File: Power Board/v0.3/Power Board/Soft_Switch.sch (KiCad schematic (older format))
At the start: 13 parts

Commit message: power board v0.3 - Raspberry Pi side only
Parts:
- removed C?: 100nF, symbol Device:C
- removed C?: 10µF, symbol Device:C
- removed C?: 1µF, symbol Device:C
- removed D?: DIODE, symbol pspice:DIODE
- removed Q? (x2): IRF7319PbF, symbol Power_Board:IRF7319PbF
- removed R? (x2): 100K, symbol Device:R
- removed R?: 330K, symbol Device:R
- removed R?: 10K, symbol Device:R
- removed R?: 1K, symbol Device:R
- removed SW?: SW_Push, symbol Switch:SW_Push
- added C10: 10µF, Capacitor_SMD:C_1210_3225Metric, symbol Device:C
- added C8: 1µF, Capacitor_SMD:C_0805_2012Metric, symbol Device:C
- added C9: 100nF, Capacitor_SMD:C_0603_1608Metric, symbol Device:C
- added D2: BAT54C, Package_TO_SOT_SMD:SOT-23, symbol Diode:BAT54C
- added D3: LED, green, LED_SMD:LED_0603_1608Metric, symbol Device:LED
- added D4: LED, red, LED_SMD:LED_0603_1608Metric, symbol Device:LED
- added L1: 300R, Inductor_SMD:L_0603_1608Metric, symbol Device:L_Core_Ferrite_Small
- added Q1: SI5504BDC, symbol Power_Board:SI5504BDC
- added Q2: DMG2305UX-7, Package_TO_SOT_SMD:SOT-23, symbol Power_Board:DMG2305UX-7
- added R10, R8: 100K, Resistor_SMD:R_0603_1608Metric, symbol Device:R
- added R11, R13: 680, Resistor_SMD:R_0603_1608Metric, symbol Device:R
- added R12, R9: 330K, Resistor_SMD:R_0603_1608Metric, symbol Device:R
- added R7: 10K, Resistor_SMD:R_0603_1608Metric, symbol Device:R
- F1: renamed from F?; footprint (none) -> Package_TO_SOT_SMD:SOT-23
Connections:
- net labels added: Power_Button, Power_Ctl_GPIO, Power_Sense_GPIO
- net labels removed: Power_GPIO
- wire segments 37 -> 53
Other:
- note added: "Drive high to keep power on."
- note added: "Low when button pressed."
- note removed: "Input w/ pull-up to read button state.\nOutput LOW to power off.\n \n"
- moved on the sheet: F1

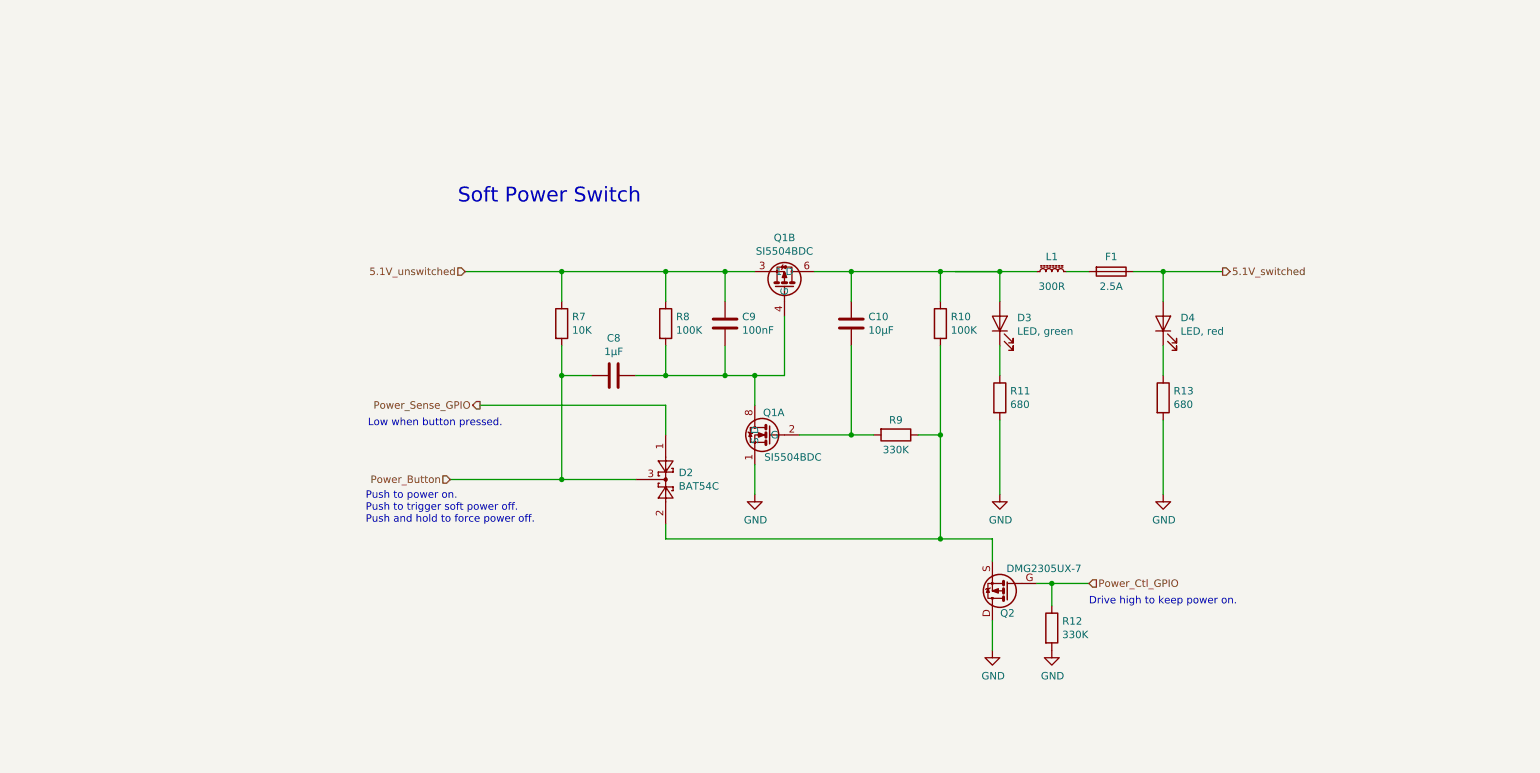
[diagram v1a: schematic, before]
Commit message: Revised soft power switch.  Now switches power to 5V regulator.
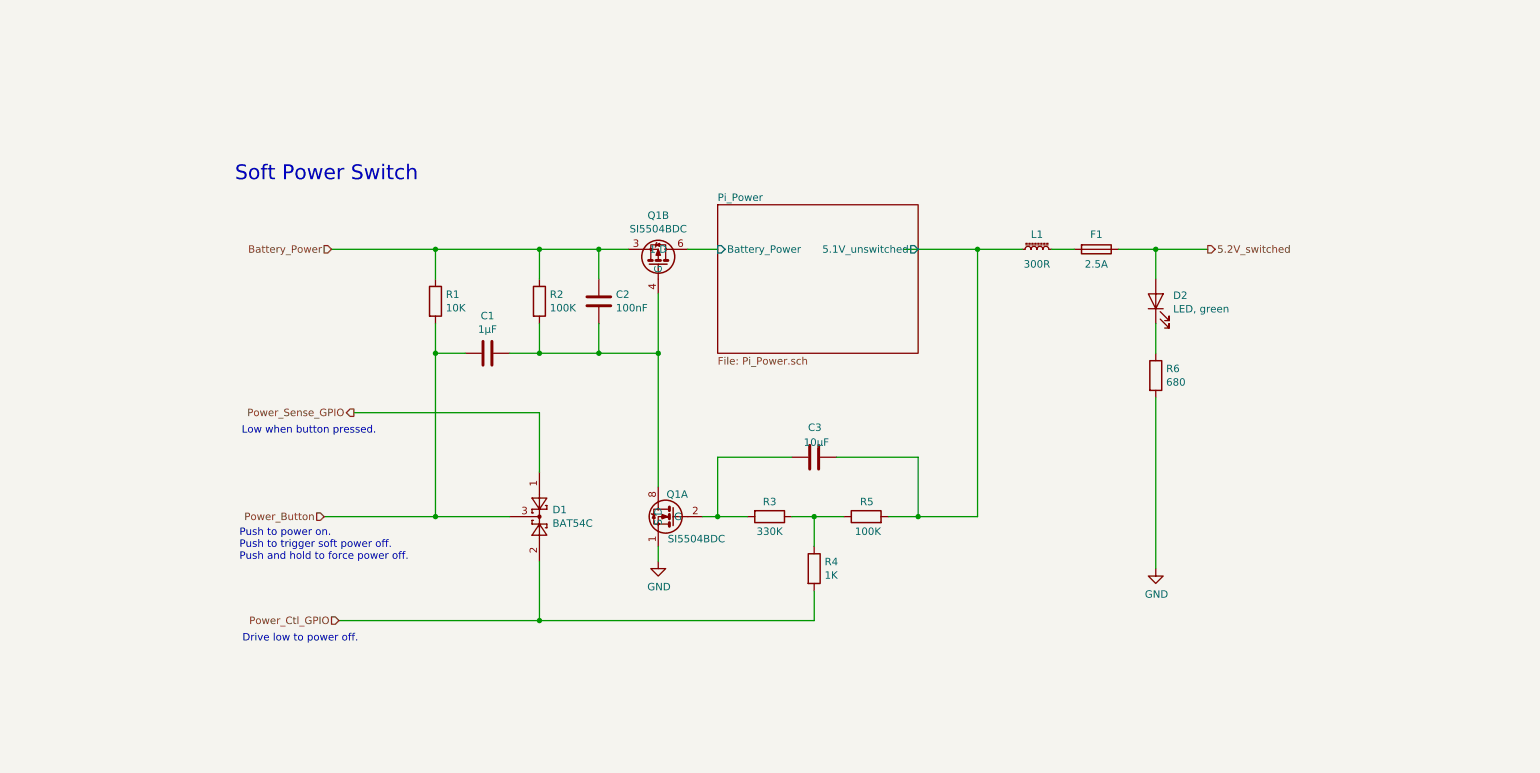
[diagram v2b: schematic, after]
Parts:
- removed D4: LED, red, LED_SMD:LED_0603_1608Metric, symbol Device:LED
- removed Q2: DMG2305UX-7, Package_TO_SOT_SMD:SOT-23, symbol Power_Board:DMG2305UX-7
- removed R12: 330K, Resistor_SMD:R_0603_1608Metric, symbol Device:R
- removed R13: 680, Resistor_SMD:R_0603_1608Metric, symbol Device:R
- added R4: 1K, Resistor_SMD:R_0603_1608Metric, symbol Device:R
- R3: renamed from R9; Part No. RX0603JR-07330K -> RC0603JR-07330K
- renumbered C8 to C1, C9 to C2, C10 to C3, D2 to D1, D3 to D2, R7 to R1, R8 to R2, R10 to R5, R11 to R6
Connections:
- net Power_Ctl_GPIO: now also D1.2, R4.2
- net at Q1.2 (G), R3.2: now also C3.1; no longer C3.2
- net 5.1V_switched renamed 5.2V_switched
- net 5.2V_switched: now also D2.2 (A)
- net 5.1V_unswitched renamed Battery_Power
- new net: C3.2, L1.1, R5.2
- new net: R3.1, R4.1, R5.1
- new net Pi_Power/Battery_Power: Q1.5 (D), Q1.6 (D)
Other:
- note added: "Drive low to power off."
- note removed: "Drive high to keep power on."
- moved on the sheet: C1, C2, C3, D1, D2, F1, L1, Q1A, Q1B, R1, R2, R3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

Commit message: Merge Pi_Power schematic into Soft_Switch.
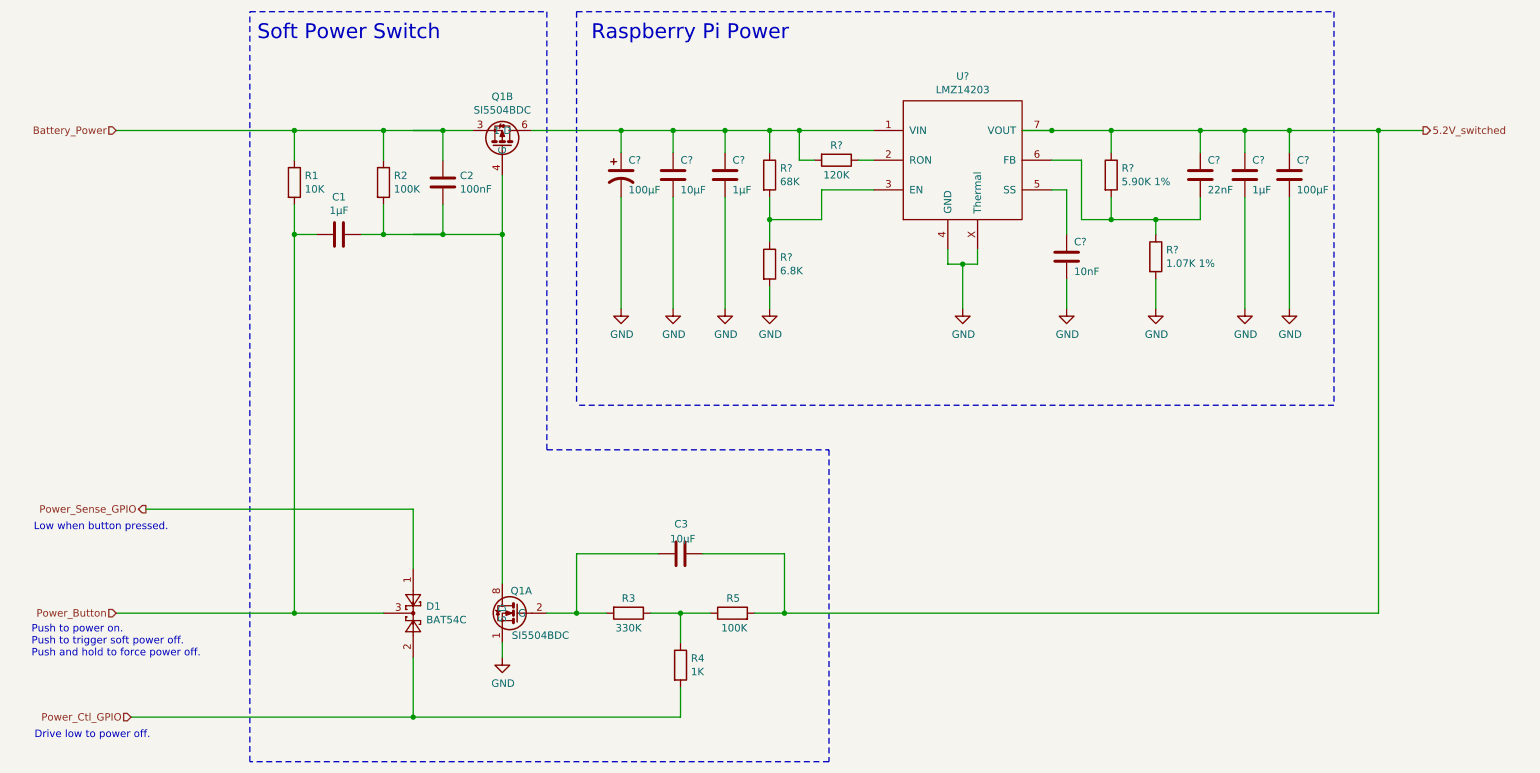
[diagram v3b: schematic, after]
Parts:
- removed D2: LED, green, LED_SMD:LED_0603_1608Metric, symbol Device:LED
- removed F1: 2.5A, Package_TO_SOT_SMD:SOT-23, symbol Device:Fuse
- removed L1: 300R, Inductor_SMD:L_0603_1608Metric, symbol Device:L_Core_Ferrite_Small
- removed R6: 680, Resistor_SMD:R_0603_1608Metric, symbol Device:R
- added C?: 10µF, Capacitor_SMD:C_1210_3225Metric, symbol Device:C
- added C? (x2): 1µF, Capacitor_SMD:C_0805_2012Metric, symbol Device:C
- added C?: 10nF, Capacitor_SMD:C_0603_1608Metric, symbol Device:C
- added C?: 22nF, Capacitor_SMD:C_0603_1608Metric, symbol Device:C
- added C?: 100µF, Capacitor_SMD:C_1210_3225Metric, symbol Device:C
- added C?: 100µF, symbol Device:CP1
- added R?: 1.07K 1%, Resistor_SMD:R_0603_1608Metric, symbol Device:R
- added R?: 5.90K 1%, Resistor_SMD:R_0603_1608Metric, symbol Device:R
- added R?: 6.8K, Resistor_SMD:R_0603_1608Metric, symbol Device:R
- added R?: 120K, Resistor_SMD:R_0603_1608Metric, symbol Device:R
- added R?: 68K, Resistor_SMD:R_0603_1608Metric, symbol Device:R
- added U?: LMZ14203, symbol Power_Board:LMZ14203
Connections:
- wire segments 47 -> 92
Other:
- note added: "Raspberry Pi Power"
- moved on the sheet: C1, C2, C3, D1, Q1A, Q1B, R1, R2, R3, R4, R5
